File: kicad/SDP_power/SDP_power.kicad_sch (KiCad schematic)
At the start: 12 parts

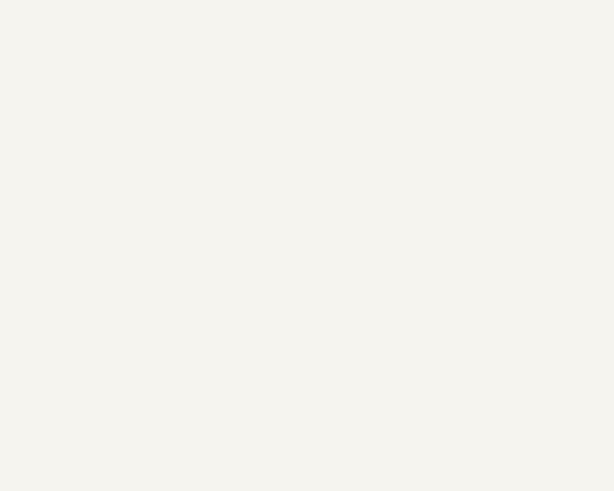
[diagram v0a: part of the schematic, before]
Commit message: PCB layout and footprint assignment fix
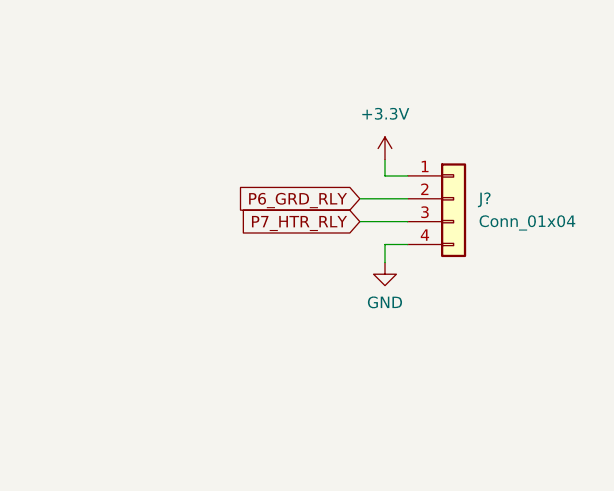
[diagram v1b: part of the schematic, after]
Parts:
- added J?: Conn_01x04, symbol Connector_Generic:Conn_01x04
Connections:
- net +3V3: now also J?.1 (Pin_1)
- net GND: now also J?.4 (Pin_4)
- net P6_GRD_RLY: now also J?.2 (Pin_2)
- net P7_HTR_RLY: now also J?.3 (Pin_3)
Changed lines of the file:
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@@
+    (stroke (width 0) (type default) (color 0 0 0 0))
+  )
+  (wire (pts (xy 226.822 49.276) (xy 232.156 49.276))
+    (stroke (width 0) (type default) (color 0 0 0 0))
+  )
+  (wire (pts (xy 226.822 46.736) (xy 232.156 46.736))
     (stroke (width 0) (type default) (color 0 0 0 0))
   )
@@
     (stroke (width 0) (type default) (color 0 0 0 0))
   )
+  (wire (pts (xy 232.156 44.196) (xy 229.616 44.196))
+    (stroke (width 0) (type default) (color 0 0 0 0))
+  )
   (wire (pts (xy 125.984 54.864) (xy 125.984 56.134))
     (stroke (width 0) (type default) (color 0 0 0 0))
   )
+  (wire (pts (xy 232.156 51.816) (xy 229.616 51.816))
+    (stroke (width 0) (type default) (color 0 0 0 0))
+  )
   (wire (pts (xy 136.144 56.134) (xy 136.144 52.324))
     (stroke (width 0) (type default) (color 0 0 0 0))
@@
     (stroke (width 0) (type default) (color 0 0 0 0))
   )
+  (wire (pts (xy 229.616 51.816) (xy 229.616 53.848))
+    (stroke (width 0) (type default) (color 0 0 0 0))
+  )
   (wire (pts (xy 91.694 66.294) (xy 91.694 63.754))
     (stroke (width 0) (type default) (color 0 0 0 0))
@@
   )
   (wire (pts (xy 49.784 56.134) (xy 49.784 57.404))
+    (stroke (width 0) (type default) (color 0 0 0 0))
+  )
+  (wire (pts (xy 229.616 44.196) (xy 229.616 42.418))
     (stroke (width 0) (type default) (color 0 0 0 0))
   )
@@
     )
   )
+  (global_label "P6_GRD_RLY" (shape input) (at 226.822 46.736 180) (fields_autoplaced)
+    (effects (font (size 1.27 1.27)) (justify right))
+    (property "Intersheet References" "${INTERSHEET_REFS}" (id 0) (at 212.7975 46.6566 0)
+      (effects (font (size 1.27 1.27)) (justify right) hide)
+    )
+  )
   (global_label "P7_HTR_RLY" (shape input) (at 117.094 47.244 180) (fields_autoplaced)
     (effects (font (size 1.27 1.27)) (justify right))
     (property "Intersheet References" "${INTERSHEET_REFS}" (id 0) (at 103.3114 47.1646 0)
+      (effects (font (size 1.27 1.27)) (justify right) hide)
+    )
+  )
+  (global_label "P7_HTR_RLY" (shape input) (at 226.822 49.276 180) (fields_autoplaced)
+    (effects (font (size 1.27 1.27)) (justify right))
+    (property "Intersheet References" "${INTERSHEET_REFS}" (id 0) (at 213.0394 49.1966 0)
       (effects (font (size 1.27 1.27)) (justify right) hide)
     )
@@
     (pin "1")
   )
+  (symbol (lib_id "power:GND") (at 229.616 53.848 0) (unit 1)
+    (in_bom yes) (on_board yes) (fields_autoplaced)
+    (property "Reference" "#PWR?" (id 0) (at 229.616 60.198 0)
+      (effects (font (size 1.27 1.27)) hide)
+    )
+    (property "Value" "GND" (id 1) (at 229.616 58.293 0))
+    (property "Footprint" "" (id 2) (at 229.616 53.848 0)
+      (effects (font (size 1.27 1.27)) hide)
+    )
+    (property "Datasheet" "" (id 3) (at 229.616 53.848 0)
+      (effects (font (size 1.27 1.27)) hide)
+    )
+    (pin "1")
+  )
+  (symbol (lib_id "power:+3.3V") (at 229.616 42.418 0) (unit 1)
+    (in_bom yes) (on_board yes) (fields_autoplaced)
+    (property "Reference" "#PWR?" (id 0) (at 229.616 46.228 0)
+      (effects (font (size 1.27 1.27)) hide)
+    )
+    (property "Value" "+3.3V" (id 1) (at 229.616 37.338 0))
+    (property "Footprint" "" (id 2) (at 229.616 42.418 0)
+      (effects (font (size 1.27 1.27)) hide)
+    )
+    (property "Datasheet" "" (id 3) (at 229.616 42.418 0)
+      (effects (font (size 1.27 1.27)) hide)
+    )
+    (pin "1")
+  )
   (symbol (lib_id "Transistor_BJT:S8050") (at 57.404 47.244 0) (unit 1)
     (in_bom yes) (on_board yes)
@@
     (pin "5")
   )
+  (symbol (lib_id "Connector_Generic:Conn_01x04") (at 237.236 46.736 0) (unit 1)
+    (in_bom yes) (on_board yes) (fields_autoplaced)
+    (property "Reference" "J?" (id 0) (at 240.03 46.7359 0)
+      (effects (font (size 1.27 1.27)) (justify left))
+    )
+    (property "Value" "Conn_01x04" (id 1) (at 240.03 49.2759 0)
+      (effects (font (size 1.27 1.27)) (justify left))
+    )
+    (property "Footprint" "" (id 2) (at 237.236 46.736 0)
+      (effects (font (size 1.27 1.27)) hide)
+    )
+    (property "Datasheet" "~" (id 3) (at 237.236 46.736 0)
+      (effects (font (size 1.27 1.27)) hide)
+    )
+    (pin "1")
+    (pin "2")
+    (pin "3")
+    (pin "4")
+  )
   (symbol (lib_id "power:+3.3V") (at 169.164 37.084 0) (unit 1)
     (in_bom yes) (on_board yes) (fields_autoplaced)
@@
       (reference "#PWR?") (unit 1) (value "GND") (footprint "")
     )
+    (path "/155fe027-7e75-4fe7-b68d-ffd5d6447ed9"
+      (reference "#PWR?") (unit 1) (value "GND") (footprint "")
+    )
+    (path "/1aef6ba8-fca2-47d7-91f4-35c2cbe6a4b9"
+      (reference "#PWR?") (unit 1) (value "+3.3V") (footprint "")
+    )
     (path "/92203fd9-b513-46a3-9b65-c104359a857e"
       (reference "#PWR?") (unit 1) (value "+3.3V") (footprint "")
@@
       (reference "J?") (unit 1) (value "Conn_01x02") (footprint "")
     )
+    (path "/89565b0f-f403-4c97-bb06-e15afb2c7188"
+      (reference "J?") (unit 1) (value "Conn_01x04") (footprint "")
+    )
     (path "/cd14c8e2-f8cd-4719-b2b7-20427483d189"
